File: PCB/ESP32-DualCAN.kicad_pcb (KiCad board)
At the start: 2 copper layers, 38.8 x 19.6 mm, 28 parts, among them J1 Molex 70553 6p, J2 Conn_01x10_Socket, J3 Conn_01x10_Socket, J4 holes, J5 pads, J6 holes, J7 pads, U1 LV2862Y, U2 ESP32-C6-SuperMini, U3 TCAN1044AV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

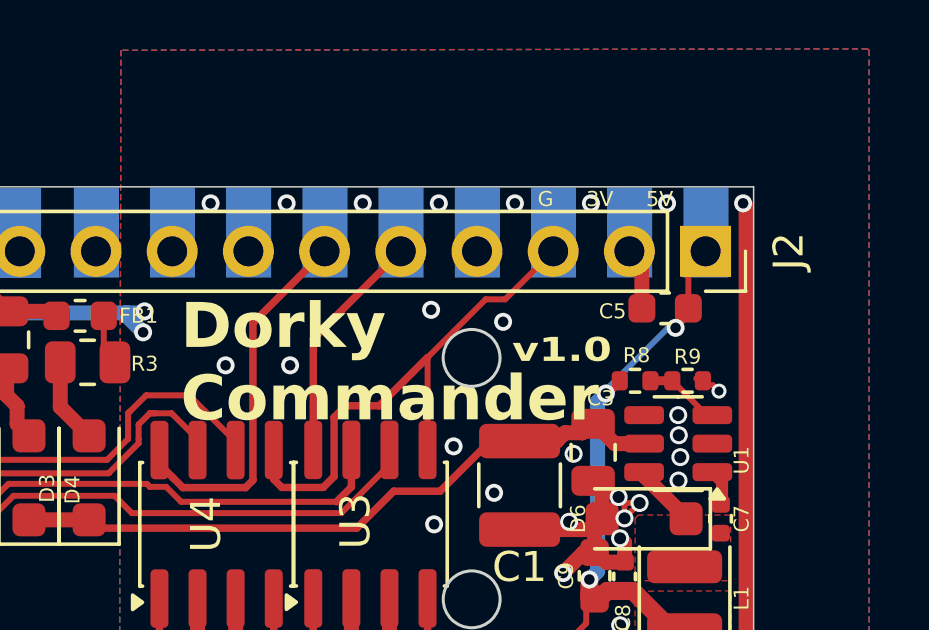
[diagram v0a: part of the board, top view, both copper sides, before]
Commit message: Fixed silk labels
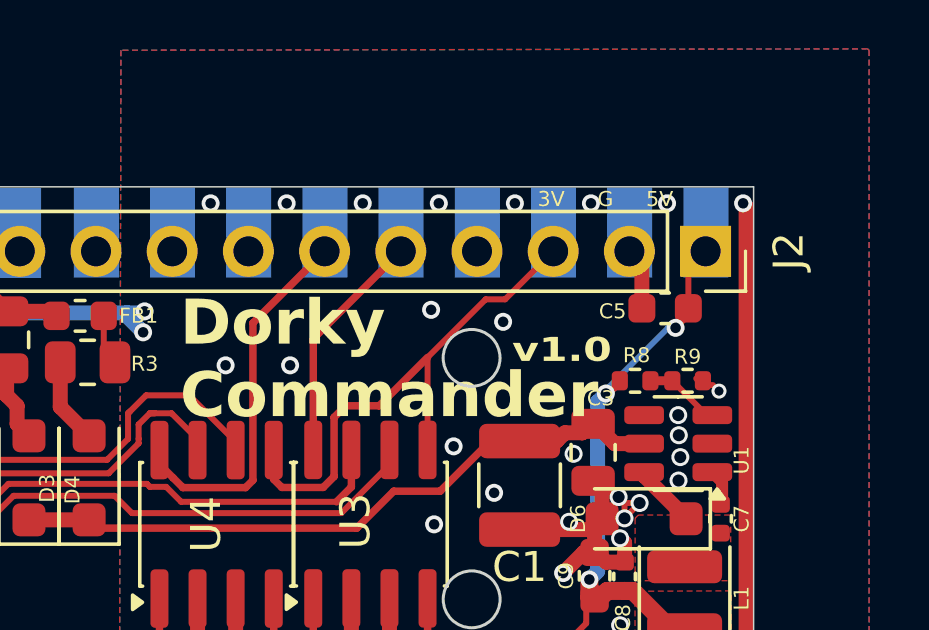
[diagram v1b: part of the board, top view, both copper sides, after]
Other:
- board text added: "3V G 5V"
- board text added: "5V G 3V"
- board text removed: "5V 3V G"
- board text removed: "G 3V 5V"
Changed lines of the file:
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@@
 		(layer "Edge.Cuts")
+	)
+	(gr_text "3V     G     5V"
+		(at 153.25 81.55 0)
+		(layer "F.SilkS")
+		(effects
+			(font
+				(size 0.5 0.5)
+				(thickness 0.125)
+			)
+			(justify left bottom)
+		)
 	)
 	(gr_text "RX    TX"
@@
 		)
 	)
-	(gr_text "G     3V     5V"
-		(at 153.25 81.55 0)
-		(layer "F.SilkS")
-		(effects
-			(font
-				(size 0.5 0.5)
-				(thickness 0.125)
-			)
-			(justify left bottom)
-		)
-	)
 	(gr_text "${REVISION}"
 		(at 152.4 86.75 0)
@@
 	)
 	(gr_text "Dorky\nCommander"
-		(at 141.35 86.7 0)
+		(at 141.33 86.59 0)
 		(layer "F.SilkS")
 		(effects
@@
 		)
 	)
+	(gr_text "5V  G  3V"
+		(at 159.65 85.15 0)
+		(layer "B.SilkS")
+		(effects
+			(font
+				(size 0.9 0.82)
+				(thickness 0.125)
+			)
+			(justify left bottom mirror)
+		)
+	)
+	(gr_text "TX RX"
+		(at 159.7 96.15 0)
+		(layer "B.SilkS")
+		(effects
+			(font
+				(size 0.9 0.9)
+				(thickness 0.125)
+			)
+			(justify left top mirror)
+		)
+	)
 	(gr_text "ESP32-C6-SuperMini\n"
 		(at 158.85 92.45 0)
@@
 	)
 	(gr_text "Vin G  1L  1H  0H 0L"
-		(at 121.9 100.4 270)
+		(at 123.095451 80.85 90)
 		(layer "B.SilkS")
 		(effects
@@
 		)
 	)
-	(gr_text "TX RX"
-		(at 159.7 96.15 0)
-		(layer "B.SilkS")
-		(effects
-			(font
-				(size 0.9 0.9)
-				(thickness 0.125)
-			)
-			(justify left top mirror)
-		)
-	)
-	(gr_text "5V  3V  G"
-		(at 159.65 85.15 0)
-		(layer "B.SilkS")
-		(effects
-			(font
-				(size 0.9 0.82)
-				(thickness 0.125)
-			)
-			(justify left bottom mirror)
-		)
-	)
 	(dimension
 		(type orthogonal)
@@
 			(keep_text_aligned yes)
 		)
-		(gr_text "1.2"
+		(gr_text "1,2"
 			(at 119.727 103.125 0)
 			(layer "Dwgs.User")
@@
 			(keep_text_aligned yes)
 		)
-		(gr_text "19.55"
+		(gr_text "19,55"
 			(at 165.05 90.625 90)
 			(layer "Cmts.User")
@@
 			(keep_text_aligned yes)
 		)
-		(gr_text "19.55"
+		(gr_text "19,55"
 			(at 114.9 90.625 90)
 			(layer "Cmts.User")
@@
 			(keep_text_aligned yes)
 		)
-		(gr_text "41.5"
+		(gr_text "41,5"
 			(at 141.2 106.85 0)
 			(layer "Cmts.User")
@@
 			(keep_text_aligned yes)
 		)
-		(gr_text "15.25"
+		(gr_text "15,25"
 			(locked yes)
 			(at 161.75 90.625 90)
